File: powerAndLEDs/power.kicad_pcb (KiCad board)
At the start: 2 copper layers, 31 parts, among them J1 Conn_Coaxial_Power, J2 GS3, J3 Screw_Terminal_01x02, SW1 SW_SPST

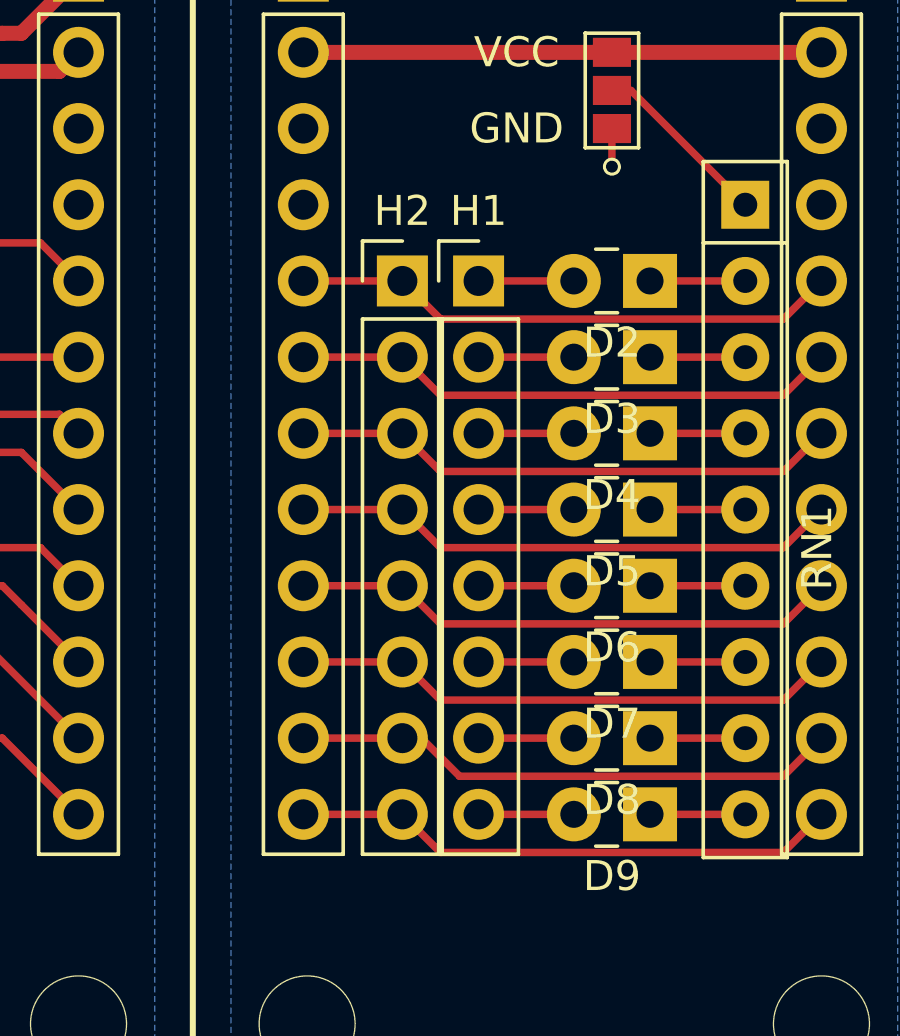
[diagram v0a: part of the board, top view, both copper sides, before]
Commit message: More update to make the libraryies use only relative paths.
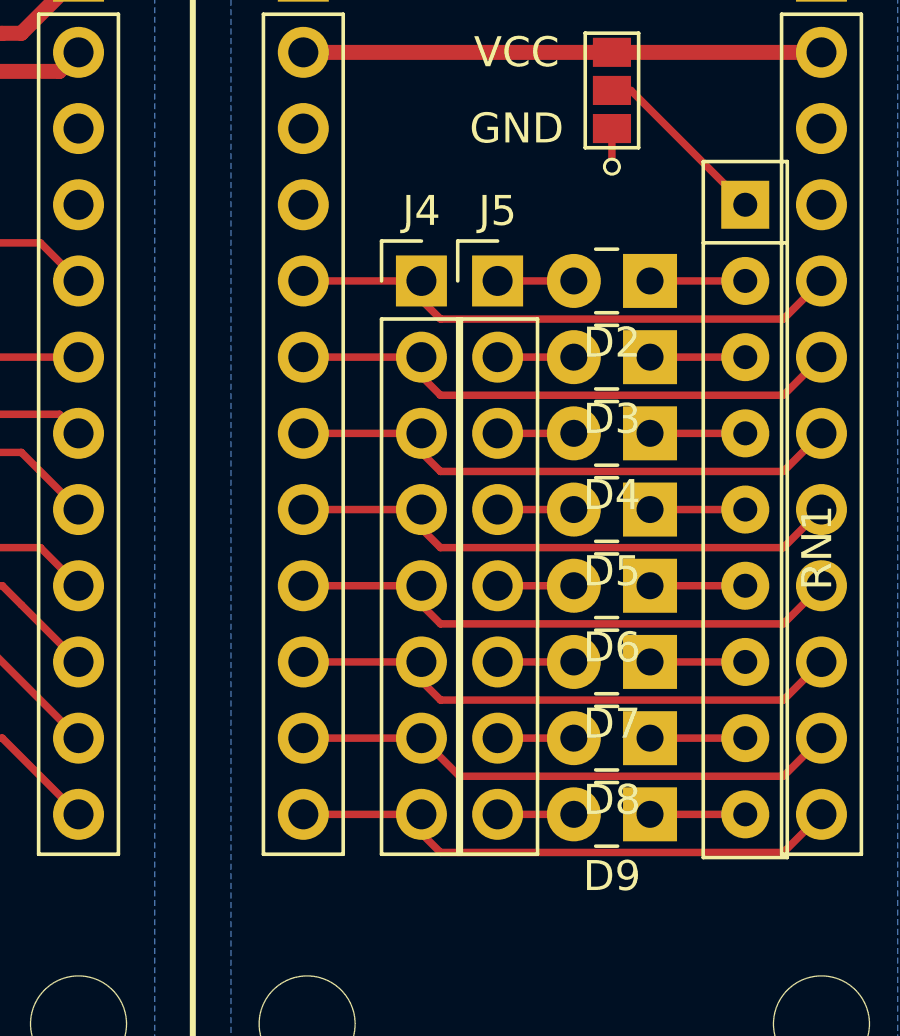
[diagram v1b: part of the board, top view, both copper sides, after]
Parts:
- removed H1: Headers8, Pin_Headers:Pin_Header_Straight_1x08_Pitch2.54mm
- removed H2: Headers8L, Pin_Headers:Pin_Header_Straight_1x08_Pitch2.54mm
- added J4: Choice, Pin_Headers:Pin_Header_Straight_1x08_Pitch2.54mm, F.Cu at (156.8, 103.5)
- added J5: Select, Pin_Headers:Pin_Header_Straight_1x08_Pitch2.54mm, F.Cu at (159.4, 103.5)
- J1: value Conn_Coaxial_Power -> Jack
- J3: value Screw_Terminal_01x02 -> Term
- TP1: value TEST -> VIN
- TP2: value TEST -> GND
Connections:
- net Earth renamed /GND
